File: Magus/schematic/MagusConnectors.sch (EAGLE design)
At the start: 43 parts, among them IC3 RC4560, J1 POWER_JACKPTH, U1 REG_S9V11F5, U2 REG_U3V12F12, U3 ICL7660, X2 1503_09, X4 1503_09

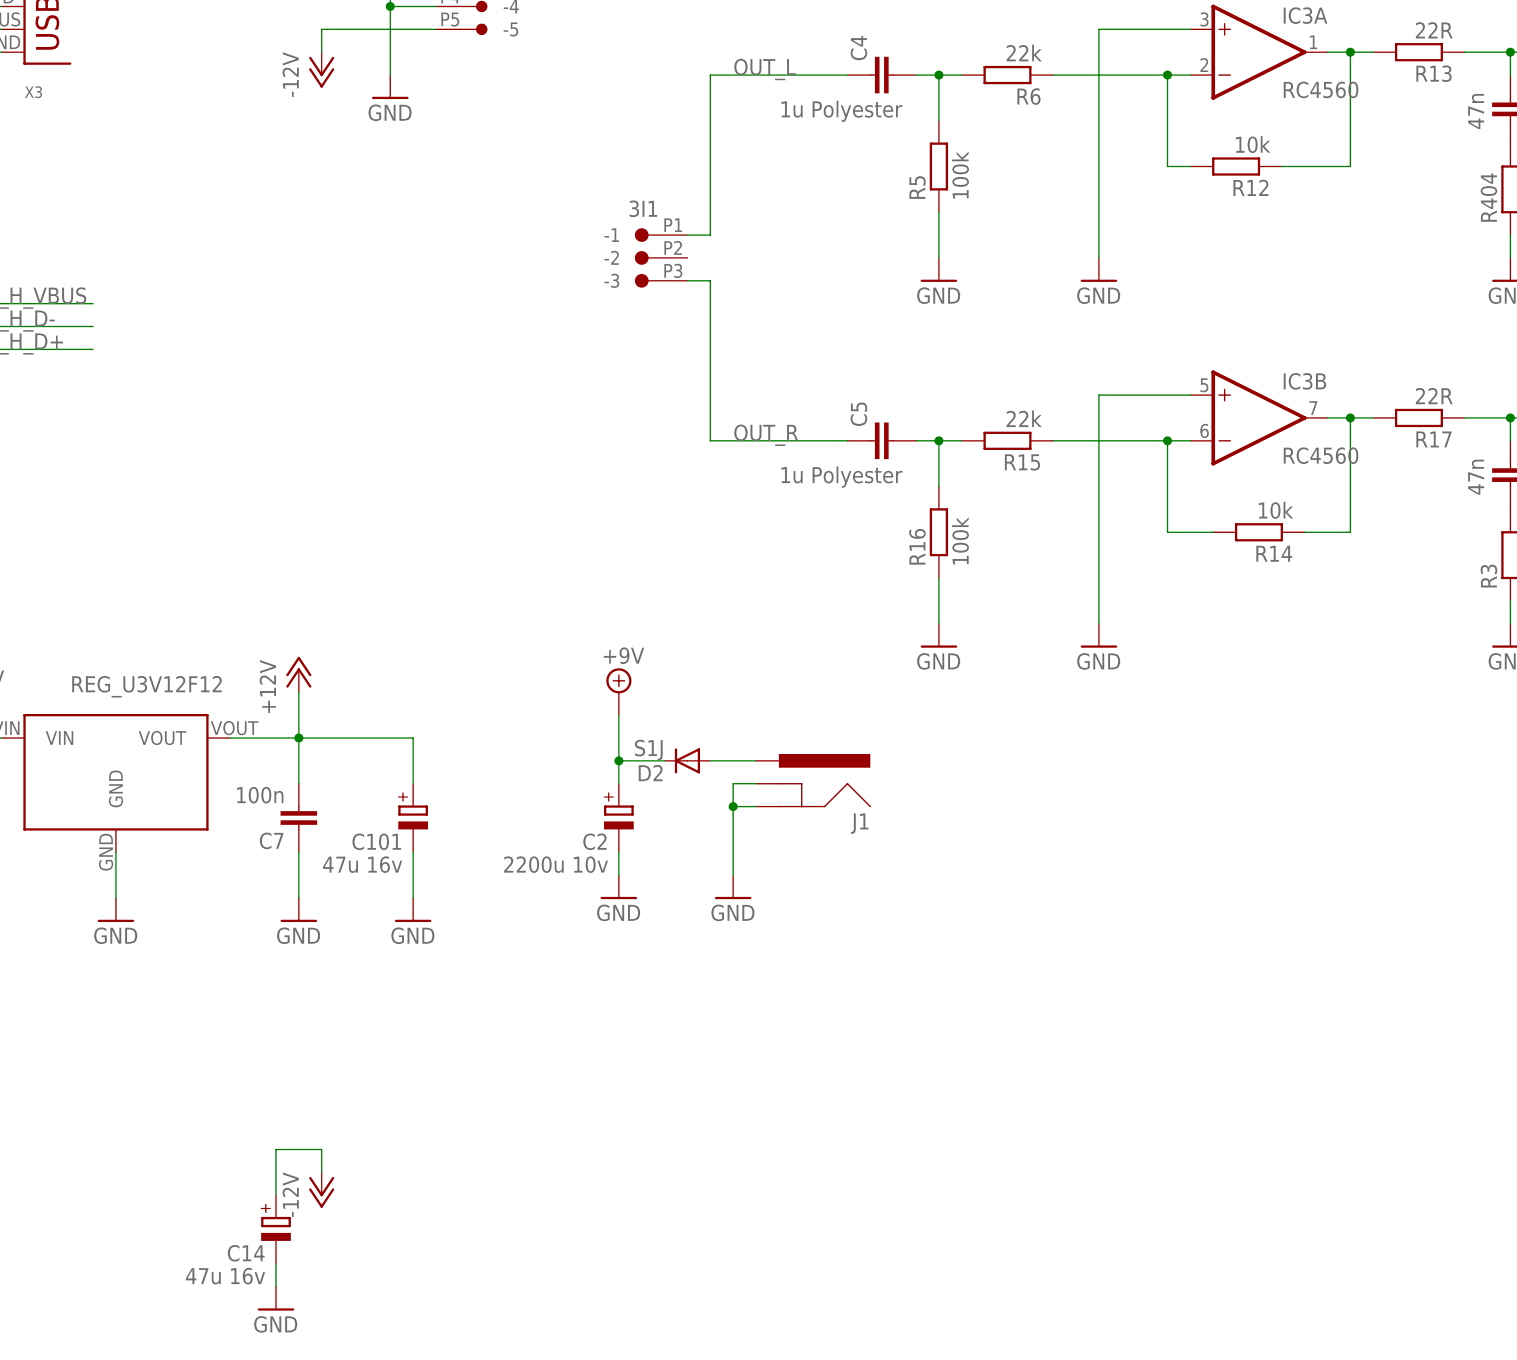
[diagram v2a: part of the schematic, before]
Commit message: added extra feedback resistors and fixed power cap polarity
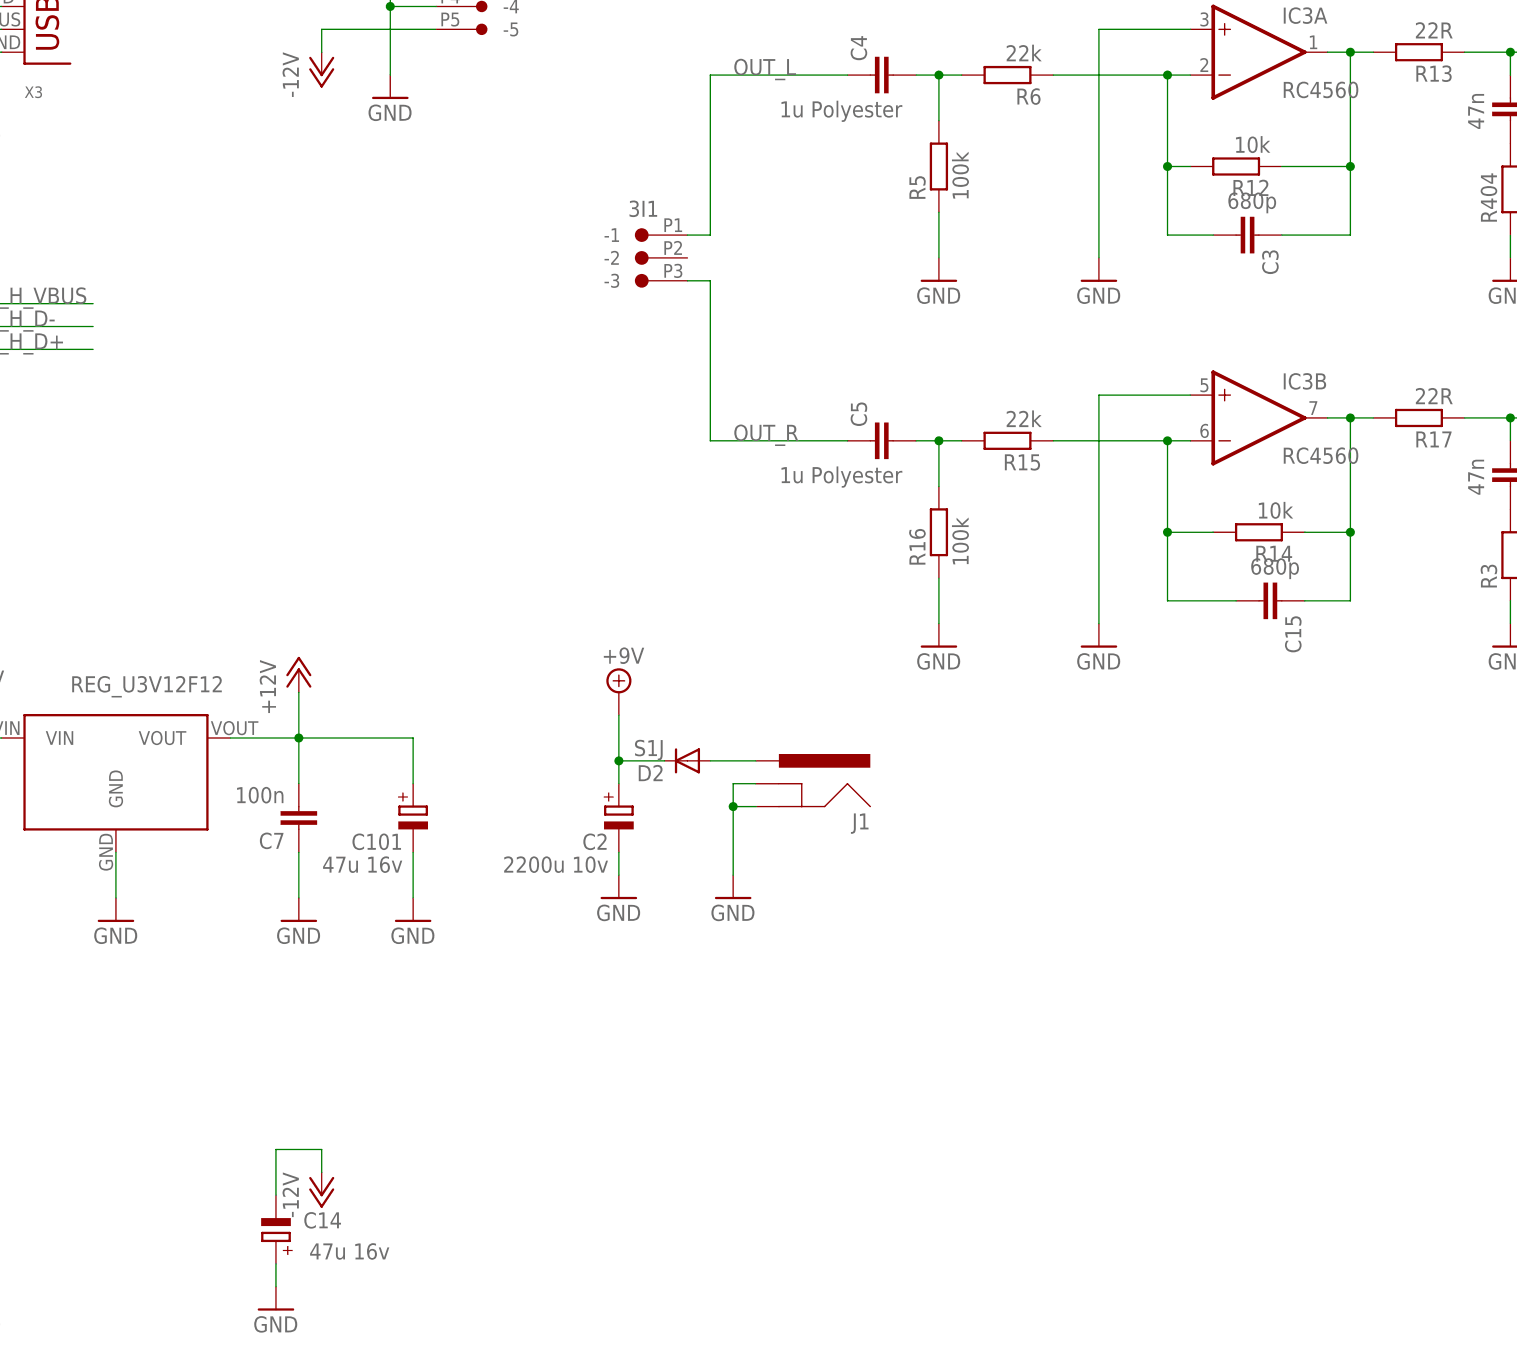
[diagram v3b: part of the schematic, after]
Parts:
- added C15, C3: 680p, Rebel:C-EUC0603
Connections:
- net -12V: now also C14.-; no longer C14.+
- net GND: now also C14.+; no longer C14.-
- net N$1: now also C15.2
- net N$19: now also C3.1
- net N$2: now also C15.1
- net N$3: now also C3.2
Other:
- moved on the sheet: C14

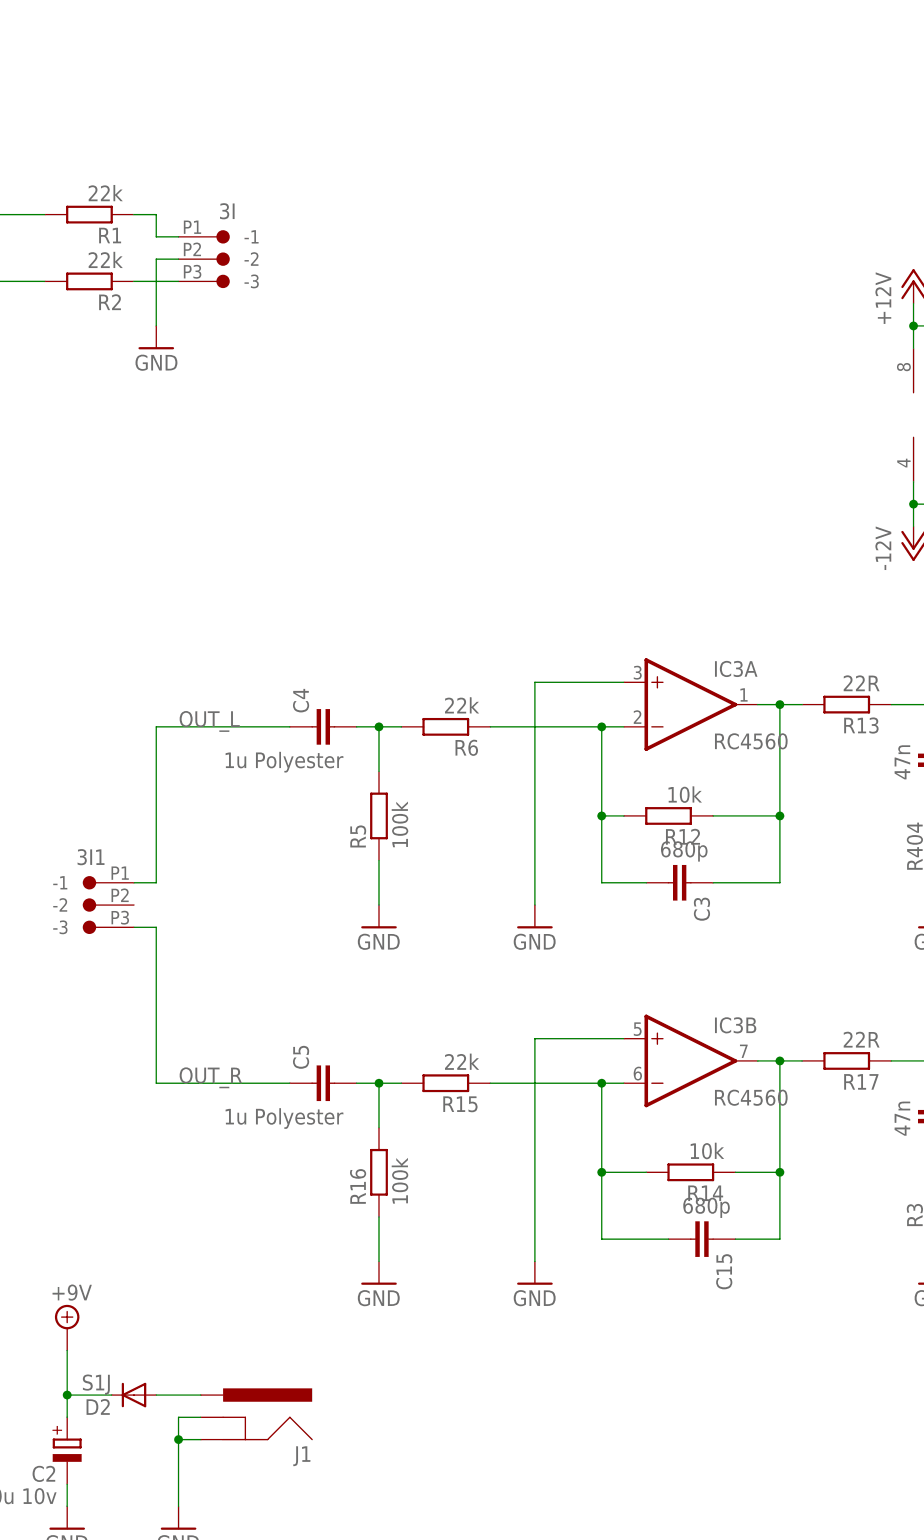
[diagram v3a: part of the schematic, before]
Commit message: added extra jack and ph-3 connector
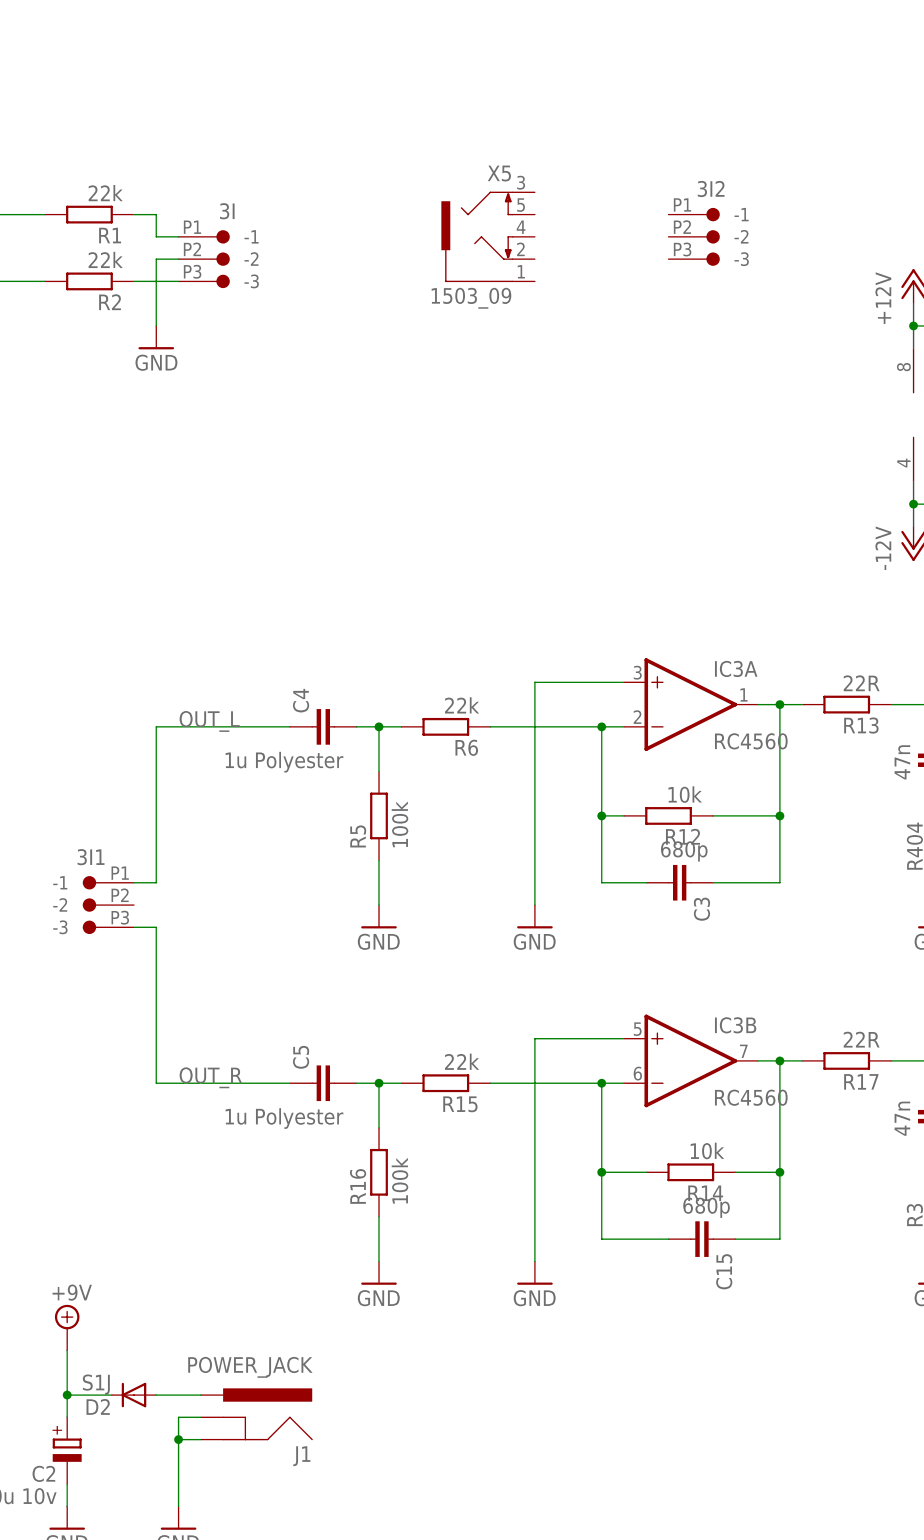
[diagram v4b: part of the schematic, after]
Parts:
- added 3I2: CON-JST_PH_3W, Rebel:CON-JST_PH_3W
- added X5: 1503_09, con-lumberg:1503_09
- J1: value POWER_JACKPTH -> POWER_JACK; device SparkFun:POWER_JACKPTH -> Rebel:POWER_JACK
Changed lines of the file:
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@@
 <?xml version="1.0" encoding="utf-8"?>
 <!DOCTYPE eagle SYSTEM "eagle.dtd">
-<eagle version="7.6.0">
+<eagle version="9.0.0">
 <drawing>
 <settings>
 <setting alwaysvectorfont="no"/>
+<setting keepoldvectorfont="yes"/>
 <setting verticaltext="up"/>
 </settings>
@@
 <part name="P+6" library="supply1" deviceset="+5V" device=""/>
 <part name="SUPPLY2" library="supply2" deviceset="+9V" device=""/>
-<part name="J1" library="SparkFun" deviceset="POWER_JACK" device="PTH" value=""/>
+<part name="J1" library="Rebel" deviceset="POWER_JACK" device="" value="POWER_JACK"/>
 <part name="D2" library="SparkFun" deviceset="DIODE" device="SMA" value="S1J"/>
 <part name="GND7" library="supply1" deviceset="GND" device=""/>
@@
 <part name="C3" library="Rebel" deviceset="C-EU" device="C0603" value="680p"/>
 <part name="C15" library="Rebel" deviceset="C-EU" device="C0603" value="680p"/>
+<part name="X5" library="con-lumberg" deviceset="1503_09" device=""/>
+<part name="3I2" library="Rebel" deviceset="CON-JST_PH_3W" device=""/>
 </parts>
 <sheets>
@@
 <attribute name="VALUE" x="194.564" y="-14.859" size="1.778" layer="96"/>
 </instance>
+<instance part="X5" gate="G$1" x="172.72" y="96.52" rot="MR0"/>
+<instance part="3I2" gate="G$1" x="193.04" y="99.06" rot="MR0"/>
 </instances>
 <busses>
